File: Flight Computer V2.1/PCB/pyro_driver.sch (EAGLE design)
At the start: 8 parts, among them Q1 VISHAY_SI7232DN-T1-GE3VISHAY_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

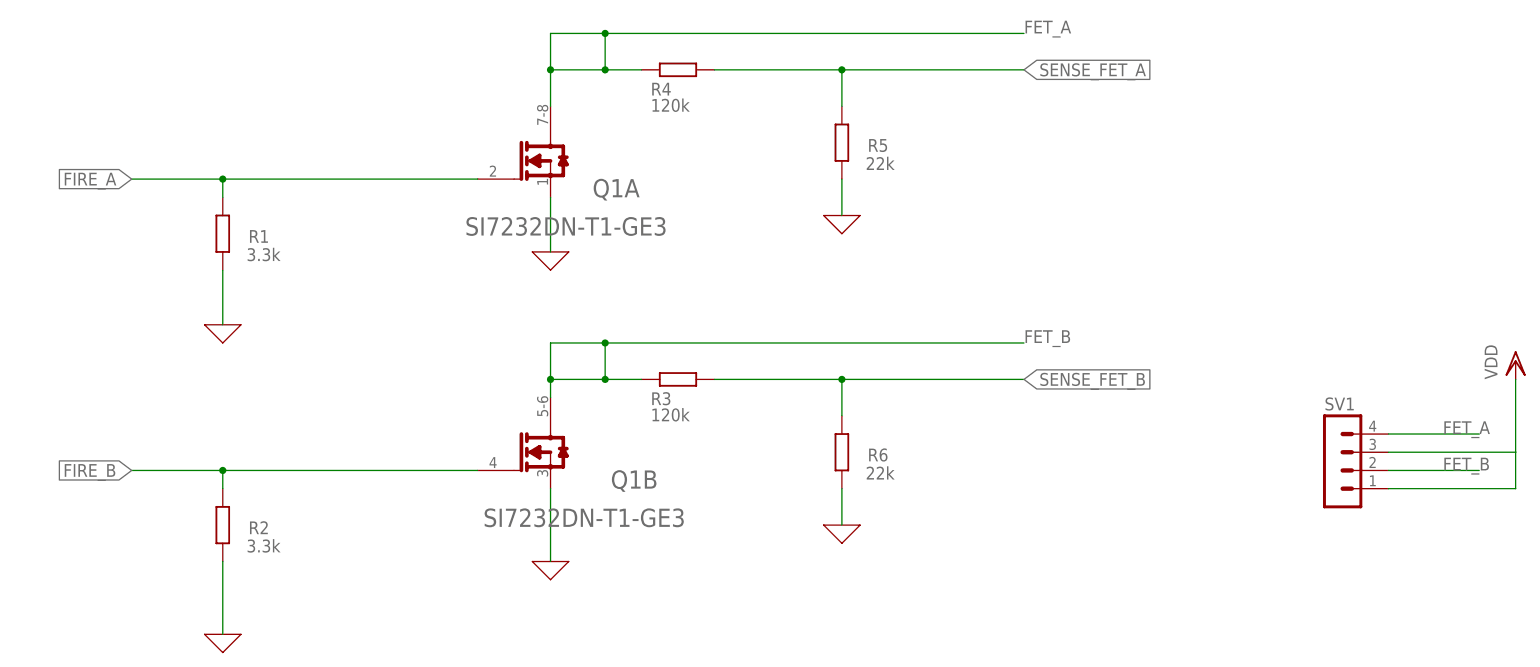
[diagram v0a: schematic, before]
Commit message: Added sensor schematic and updated pyro driver schematic
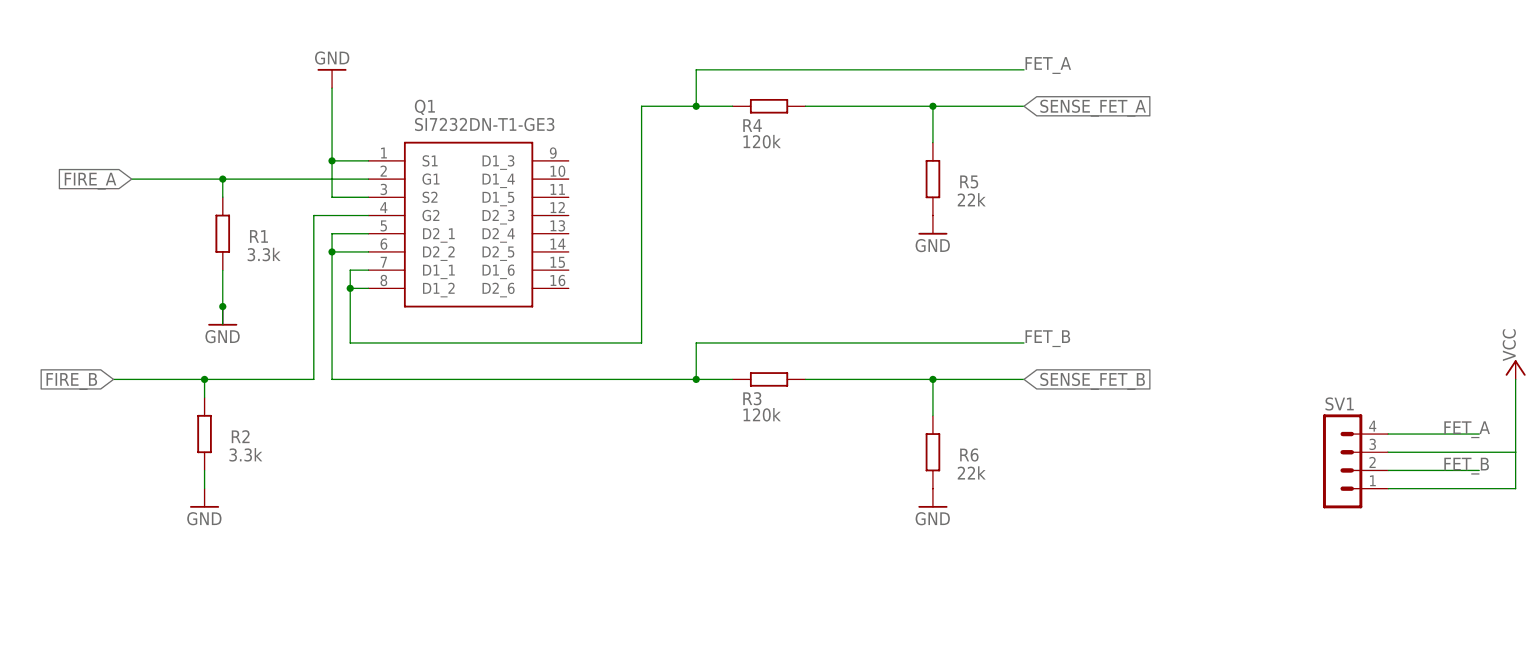
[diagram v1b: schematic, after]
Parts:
- Q1: value VISHAY_SI7232DN-T1-GE3VISHAY_SI7232DN-T1-GE3_0_0 -> SI7232DN-T1-GE3; device Vishay - SI7232DN-T1-GE3:VISHAY_SI7232DN-T1-GE3VISHAY_SI7232DN-T1-GE3_0_0 -> SI7232DN-T1-GE3:SI7232DN-T1-GE3
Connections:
- net VDD renamed VDRIVE
- removed net 0: Q1A.S1, Q1B.S2, R1.1, R2.1, R5.1, R6.1
- new net GND: Q1.S1, Q1.S2, R1.1, R2.1, R5.1, R6.1
- net FET_A: now also Q1.D1_1, Q1.D1_2; no longer Q1A.D1
- net FET_B: now also Q1.D2_1, Q1.D2_2; no longer Q1B.D2
- net FIRE_A: now also Q1.G1; no longer Q1A.G1
- net FIRE_B: now also Q1.G2; no longer Q1B.G2
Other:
- moved on the sheet: R2, R3, R4, R5, R6
